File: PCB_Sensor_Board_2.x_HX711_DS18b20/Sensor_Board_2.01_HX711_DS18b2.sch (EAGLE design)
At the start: 23 parts

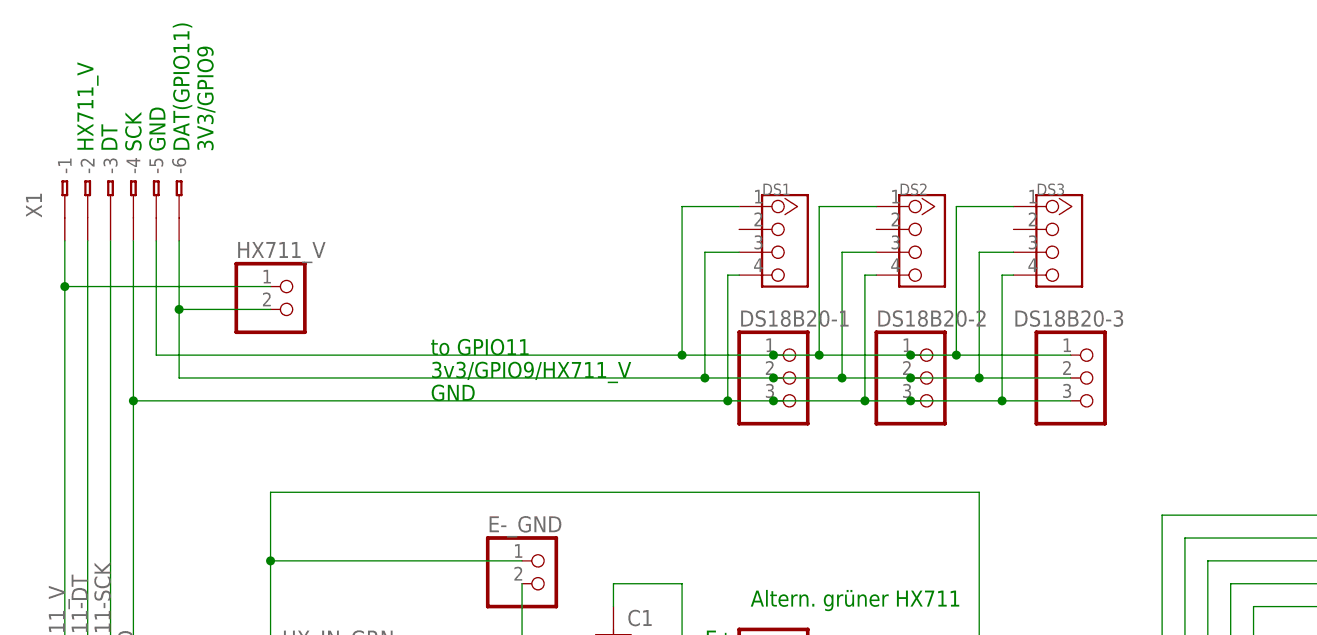
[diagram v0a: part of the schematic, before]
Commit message: add_ 1x DS18B20 TO-92
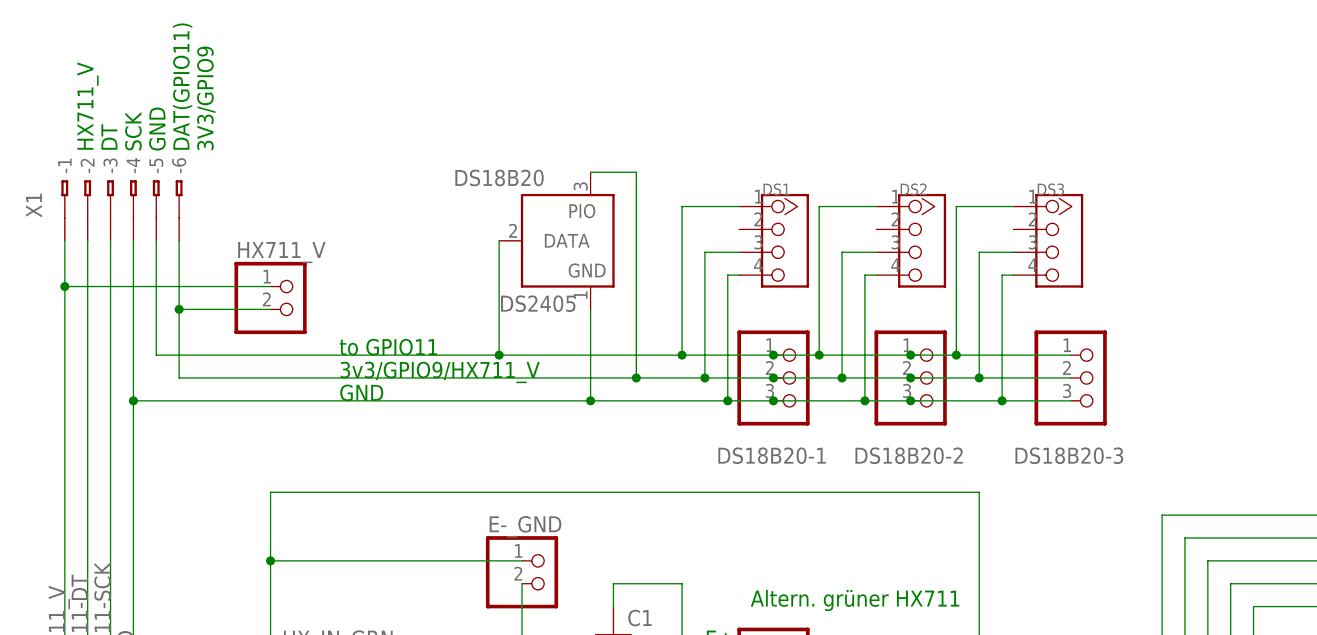
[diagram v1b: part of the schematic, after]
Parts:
- added DS18B20: DS2405, maxim:DS2405
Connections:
- net 3V3: now also DS18B20.PIO
- net DS18B20_DATA_GPIO11_PIN23: now also DS18B20.DATA
- net GND: now also DS18B20.GND
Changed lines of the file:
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@@
 <part name="R2" library="rcl" library_urn="urn:adsk.eagle:library:334" deviceset="R-EU_" device="0207/10" package3d_urn="urn:adsk.eagle:package:23491/2" value="100Ohm"/>
 <part name="C_ON/OFF" library="pinhead" library_urn="urn:adsk.eagle:library:325" deviceset="PINHD-1X2" device="" package3d_urn="urn:adsk.eagle:package:22435/2"/>
+<part name="DS18B20" library="maxim" library_urn="urn:adsk.eagle:library:269" deviceset="DS2405" device="" package3d_urn="urn:adsk.eagle:package:17530/1"/>
 </parts>
 <sheets>
 <sheet>
 <plain>
-<text x="-129.54" y="45.72" size="1.778" layer="91">3v3/GPIO9/HX711_V</text>
+<text x="-139.7" y="45.72" size="1.778" layer="91">3v3/GPIO9/HX711_V</text>
 <text x="-135.89" y="-41.402" size="1.778" layer="91" grouprefs="PFLAUME">VCC 3,3V
 DT
@@
 SCK
 VCC 3,3V</text>
-<text x="-129.54" y="43.18" size="1.778" layer="91">GND</text>
-<text x="-129.54" y="48.26" size="1.778" layer="91">to GPIO11</text>
+<text x="-139.7" y="43.18" size="1.778" layer="91">GND</text>
+<text x="-139.7" y="48.26" size="1.778" layer="91">to GPIO11</text>
 <text x="-29.21" y="53.34" size="1.778" layer="91">Erweiterungsboard f. HoneyPI HAT 2.0
 Passend für das Gehäuse Rose Nr: 01.06 10 03
@@
 <instances>
 <instance part="DS18B20-3" gate="A" x="-55.88" y="45.72" smashed="yes">
-<attribute name="NAME" x="-64.77" y="51.435" size="1.778" layer="95"/>
+<attribute name="NAME" x="-64.77" y="36.195" size="1.778" layer="95"/>
 <attribute name="VALUE" x="-62.23" y="38.1" size="1.778" layer="96"/>
 </instance>
 <instance part="DS18B20-2" gate="A" x="-73.66" y="45.72" smashed="yes">
-<attribute name="NAME" x="-80.01" y="51.435" size="1.778" layer="95"/>
+<attribute name="NAME" x="-82.55" y="36.195" size="1.778" layer="95"/>
 <attribute name="VALUE" x="-80.01" y="38.1" size="1.778" layer="96"/>
 </instance>
 <instance part="DS18B20-1" gate="A" x="-88.9" y="45.72" smashed="yes">
-<attribute name="NAME" x="-95.25" y="51.435" size="1.778" layer="95"/>
+<attribute name="NAME" x="-97.79" y="36.195" size="1.778" layer="95"/>
 <attribute name="VALUE" x="-95.25" y="38.1" size="1.778" layer="96"/>
 </instance>
@@
 <attribute name="NAME" x="-121.158" y="-41.783" size="1.778" layer="95"/>
 <attribute name="VALUE" x="-107.95" y="-40.64" size="1.778" layer="96" rot="R180"/>
+</instance>
+<instance part="DS18B20" gate="G$1" x="-114.3" y="60.96" smashed="yes">
+<attribute name="NAME" x="-127" y="67.056" size="1.778" layer="95"/>
+<attribute name="VALUE" x="-121.92" y="53.086" size="1.778" layer="96"/>
 </instance>
 </instances>
@@
 <wire x1="-68.58" y1="59.69" x2="-68.58" y2="45.72" width="0.1524" layer="91"/>
 <junction x="-68.58" y="45.72"/>
-<wire x1="-99.06" y1="45.72" x2="-157.48" y2="45.72" width="0.1524" layer="91"/>
+<wire x1="-99.06" y1="45.72" x2="-106.68" y2="45.72" width="0.1524" layer="91"/>
 <junction x="-99.06" y="45.72"/>
 <pinref part="HX711_V" gate="G$1" pin="2"/>
+<wire x1="-106.68" y1="45.72" x2="-157.48" y2="45.72" width="0.1524" layer="91"/>
 <wire x1="-157.48" y1="53.34" x2="-157.48" y2="45.72" width="0.1524" layer="91"/>
 <wire x1="-147.32" y1="53.34" x2="-157.48" y2="53.34" width="0.1524" layer="91"/>
@@
 <wire x1="-157.48" y1="53.34" x2="-157.48" y2="60.96" width="0.1524" layer="91"/>
 <pinref part="X1" gate="G$1" pin="B-6"/>
+<pinref part="DS18B20" gate="G$1" pin="PIO"/>
+<wire x1="-111.76" y1="68.58" x2="-106.68" y2="68.58" width="0.1524" layer="91"/>
+<wire x1="-106.68" y1="68.58" x2="-106.68" y2="45.72" width="0.1524" layer="91"/>
+<junction x="-106.68" y="45.72"/>
 </segment>
 </net>
@@
 <wire x1="-96.52" y1="57.15" x2="-96.52" y2="43.18" width="0.1524" layer="91"/>
 <junction x="-96.52" y="43.18"/>
-<wire x1="-162.56" y1="43.18" x2="-96.52" y2="43.18" width="0.1524" layer="91"/>
+<wire x1="-162.56" y1="43.18" x2="-111.76" y2="43.18" width="0.1524" layer="91"/>
+<wire x1="-111.76" y1="43.18" x2="-96.52" y2="43.18" width="0.1524" layer="91"/>
 <wire x1="-162.56" y1="12.7" x2="-162.56" y2="43.18" width="0.1524" layer="91"/>
 <label x="-162.56" y="12.7" size="1.778" layer="95" rot="R90"/>
@@
 <junction x="-48.26" y="5.08"/>
 <pinref part="X1" gate="G$1" pin="B-4"/>
+<pinref part="DS18B20" gate="G$1" pin="GND"/>
+<wire x1="-111.76" y1="53.34" x2="-111.76" y2="43.18" width="0.1524" layer="91"/>
+<junction x="-111.76" y="43.18"/>
 </segment>
 </net>
@@
 <wire x1="-91.44" y1="48.26" x2="-101.6" y2="48.26" width="0.1524" layer="91"/>
 <pinref part="DS3" gate="G$1" pin="1"/>
-<wire x1="-101.6" y1="48.26" x2="-160.02" y2="48.26" width="0.1524" layer="91"/>
+<wire x1="-101.6" y1="48.26" x2="-121.92" y2="48.26" width="0.1524" layer="91"/>
+<wire x1="-121.92" y1="48.26" x2="-160.02" y2="48.26" width="0.1524" layer="91"/>
 <wire x1="-64.77" y1="64.77" x2="-71.12" y2="64.77" width="0.1524" layer="91"/>
 <wire x1="-71.12" y1="64.77" x2="-71.12" y2="48.26" width="0.1524" layer="91"/>
@@
 <wire x1="-160.02" y1="48.26" x2="-160.02" y2="60.96" width="0.1524" layer="91"/>
 <pinref part="X1" gate="G$1" pin="B-5"/>
-</segment>
-</net>
+<pinref part="DS18B20" gate="G$1" pin="DATA"/>
+<wire x1="-121.92" y1="60.96" x2="-121.92" y2="48.26" width="0.1524" layer="91"/>
+<junction x="-121.92" y="48.26"/>
+</segment>
+</net>
